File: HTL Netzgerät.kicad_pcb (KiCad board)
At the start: 2 copper layers, 139.7 x 65.7 mm, 62 parts, among them T1 BC547, T2 BC547, T3 BC547, T4 BC547, T5 BC547, T6 BC557, T7 BC557, T8 BC639, X1 AUX1_AC1, X10 C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

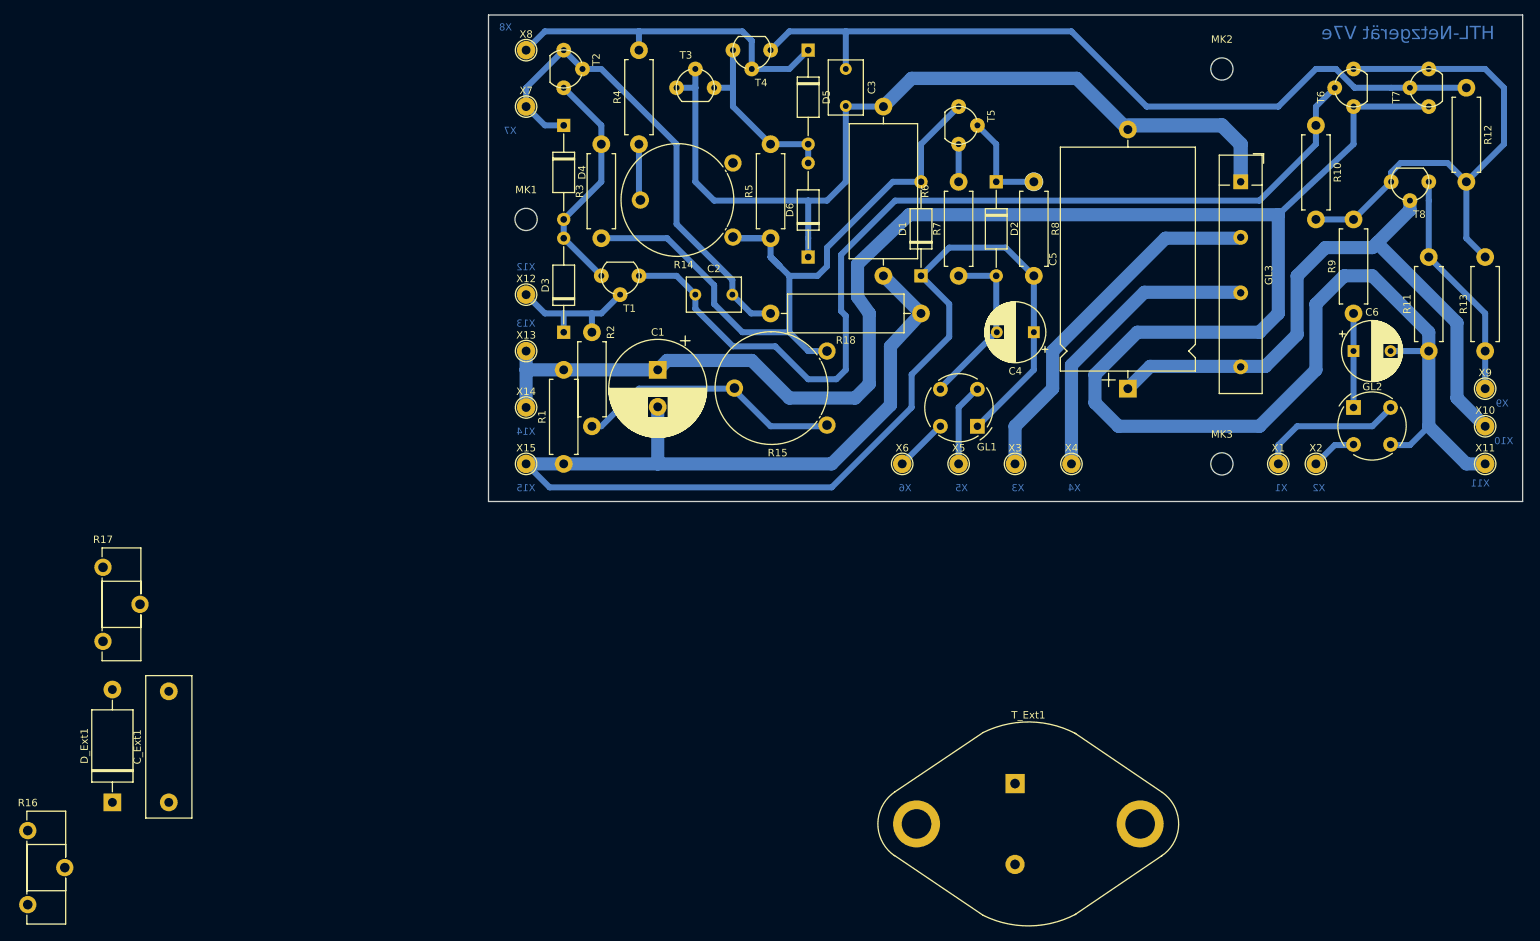
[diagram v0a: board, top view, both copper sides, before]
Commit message: Libs und TODOs aktualisiert
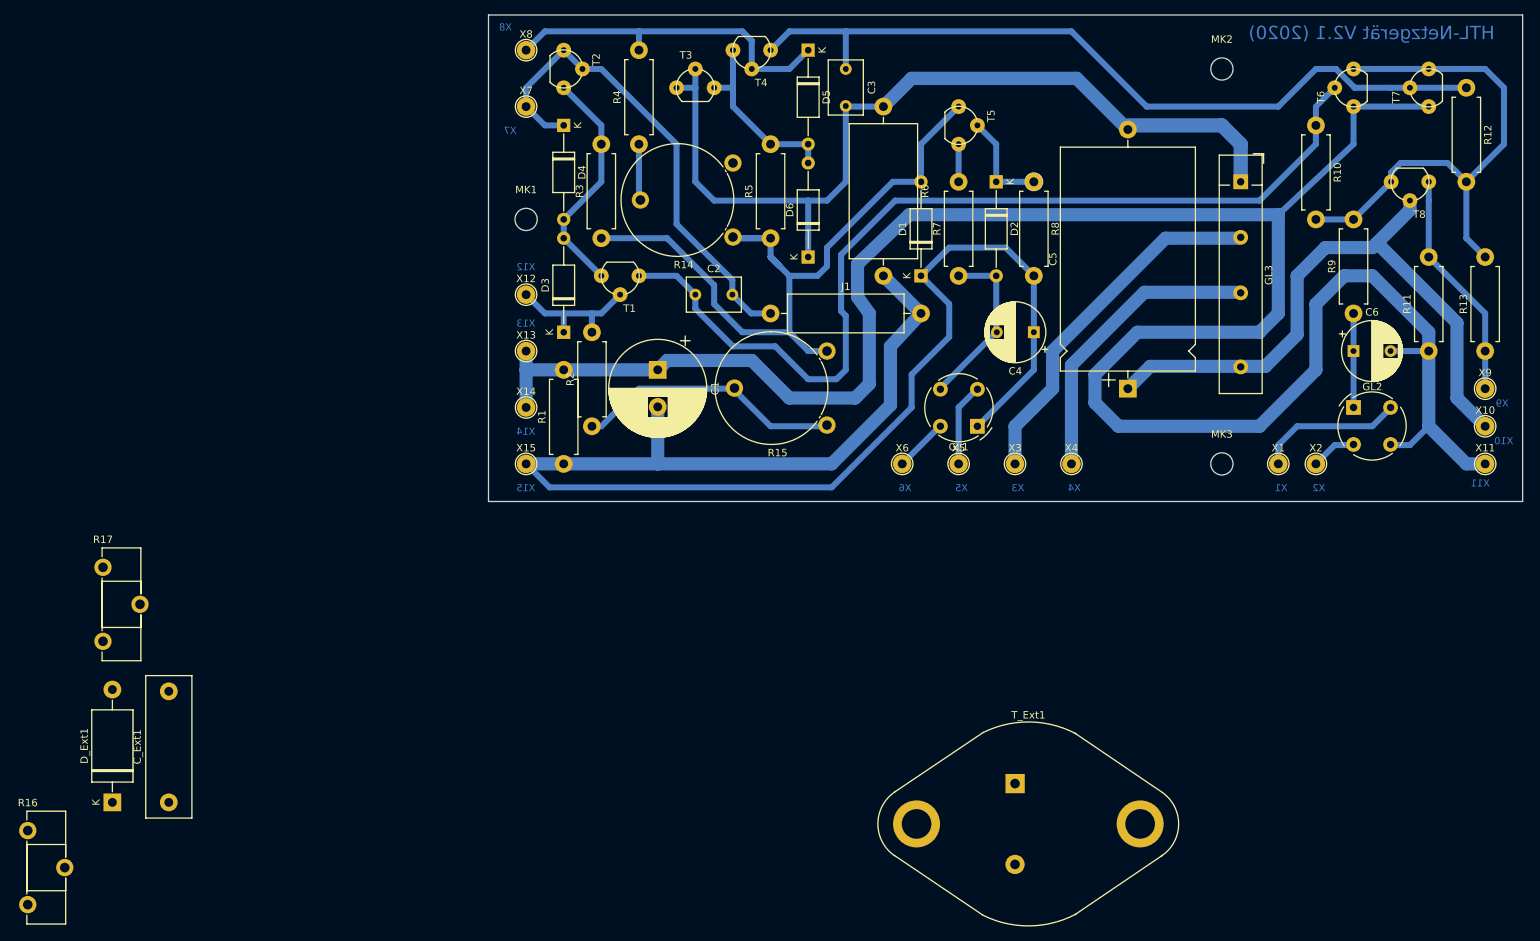
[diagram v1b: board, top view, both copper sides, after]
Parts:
- removed R18: 0R/20.32mm, v5_Resistor_THT:R_Axial_DIN0516_L15.5mm_D5.0mm_P20.32mm_Horizontal
- added J1: 0.7/20.32mm, Resistor_THT:R_Axial_DIN0516_L15.5mm_D5.0mm_P20.32mm_Horizontal, F.Cu at (116.8, 112.5)
- C1: footprint v5_Capacitor_THT:CP_Radial_D13.0mm_P5.00mm -> Capacitor_THT:CP_Radial_D13.0mm_P5.00mm
- C2, C3: footprint v5_Capacitor_THT:C_Rect_L7.2mm_W4.5mm_P5.00mm_FKS2_FKP2_MKS2_MKP2 -> Capacitor_THT:C_Rect_L7.2mm_W4.5mm_P5.00mm_FKS2_FKP2_MKS2_MKP2
- C4, C6: footprint v5_Capacitor_THT:CP_Radial_D8.0mm_P5.00mm -> Capacitor_THT:CP_Radial_D8.0mm_P5.00mm
- C5: footprint v5_Capacitor_THT:CP_Axial_L30.0mm_D18.0mm_P35.00mm_Horizontal -> Capacitor_THT:CP_Axial_L30.0mm_D18.0mm_P35.00mm_Horizontal
- C_Ext1: footprint v5_Capacitor_THT:C_Rect_L19.0mm_W6.0mm_P15.00mm_MKS4 -> Capacitor_THT:C_Rect_L19.0mm_W6.0mm_P15.00mm_MKS4
- D1, D2, D3, D4, D5, D6: footprint v5_Diode_THT:D_A-405_P12.70mm_Horizontal -> Diode_THT:D_A-405_P12.70mm_Horizontal
- D_Ext1: footprint v5_Diode_THT:D_DO-27_P15.24mm_Horizontal -> Diode_THT:D_DO-27_P15.24mm_Horizontal
- GL1, GL2: footprint v5_Diode_THT:Diode_Bridge_Round_D9.0mm -> Diode_THT:Diode_Bridge_Round_D9.0mm
- GL3: footprint v5_Diode_THT:Diode_Bridge_32.0x5.6x17.0mm_P10.0mm_P7.5mm -> Diode_THT:Diode_Bridge_32.0x5.6x17.0mm_P10.0mm_P7.5mm
- MK1, MK2, MK3: footprint v5_MountingHole:MountingHole_3mm -> MountingHole:MountingHole_3mm
- R1, R10, R11, R12, R13, R2, R3, R4, R5, R7, R8, R9: footprint v5_Resistor_THT:R_Axial_DIN0411_L9.9mm_D3.6mm_P12.70mm_Horizontal -> Resistor_THT:R_Axial_DIN0411_L9.9mm_D3.6mm_P12.70mm_Horizontal
- R14, R15: footprint v5_Potentiometer_THT:Potentiometer_Piher_PT-15-V02_Vertical -> Potentiometer_THT:Potentiometer_Piher_PT-15-V02_Vertical
- R16, R17: footprint v5_Potentiometer_THT:Potentiometer_Piher_PT-15-H25_Horizontal -> Potentiometer_THT:Potentiometer_Piher_PT-15-H25_Horizontal
- R6: footprint v5_Resistor_THT:R_Axial_DIN0918_L18.0mm_D9.0mm_P22.86mm_Horizontal -> Resistor_THT:R_Axial_DIN0918_L18.0mm_D9.0mm_P22.86mm_Horizontal
- T_Ext1: footprint v5_Package_TO_SOT_THT:TO-3 -> Package_TO_SOT_THT:TO-3
- X1, X10, X11, X12, X13, X14, X15, X2, X3, X4, X5, X6, X7, X8, X9: footprint v5_TestPoint:TestPoint_THTPad_D2.5mm_Drill1.2mm -> TestPoint:TestPoint_THTPad_D2.5mm_Drill1.2mm
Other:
- board text added: "HTL-Netzgerät V2.1 (2020)"
- board text removed: "HTL-Netzgerät V7e"

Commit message: Einige Korrekturen eingepflegt für Version 2.1
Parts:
- MK1, MK2, MK3: footprint MountingHole:MountingHole_3mm -> MountingHole:MountingHole_3.2mm_M3
- R14, R15: footprint Potentiometer_THT:Potentiometer_Piher_PT-15-V02_Vertical -> HTL_Netzgeraet:Potentiometer_Piher_PT-15-V02_Vertical
- R6: footprint Resistor_THT:R_Axial_DIN0918_L18.0mm_D9.0mm_P22.86mm_Horizontal -> Resistor_THT:R_Axial_DIN0922_L20.0mm_D9.0mm_P30.48mm_Horizontal
- T1, T2, T3, T4, T5, T6, T7, T8: footprint HTL Netzgerät:TO-92 -> HTL_Netzgeraet:TO-92
- X1, X10, X11, X12, X13, X14, X15, X2, X3, X4, X5, X6, X7, X8, X9: footprint TestPoint:TestPoint_THTPad_D2.5mm_Drill1.2mm -> HTL_Netzgeraet:TestPoint_THTPad_D2.5mm_Drill1.25mm
- moved X3 7.62 mm to (157.4, 132.8)
- moved X4 7.62 mm to (149.8, 132.8)
- moved X1 5.08 mm to (190.4, 132.8)
- moved X2 5.08 mm to (185.3, 132.8)
- renumbered R16 to P1, R17 to P2
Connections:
- J1 pad 1: /V_U_Ref -> /0V
- J1 pad 2: /0V -> /V_U_Ref
- X1 pad 1: Net-(GL2-Pad4) -> Net-(GL2-Pad2)
- X2 pad 1: Net-(GL2-Pad2) -> Net-(GL2-Pad4)
- X3 pad 1: Net-(GL3-Pad2) -> Net-(GL3-Pad3)
- X4 pad 1: Net-(GL3-Pad3) -> Net-(GL3-Pad2)
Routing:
- net Net-(R14-Pad2): track 7.62 -> 10.4 mm
- net Net-(R15-Pad2): track 36.0 -> 38.7 mm
- net Net-(GL2-Pad4): track 19.9 -> 18.4 mm

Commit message: Weitere Verbesserungen, Drahtbrücke, Texte, siehe Changelog
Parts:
- GL3: footprint Diode_THT:Diode_Bridge_32.0x5.6x17.0mm_P10.0mm_P7.5mm -> HTL_Netzgeraet:Brueckengleichrichter_p7.4-7.2-9.5mm
- J1: footprint Resistor_THT:R_Axial_DIN0516_L15.5mm_D5.0mm_P20.32mm_Horizontal -> HTL_Netzgeraet:Drahtbruecke_d0.7mm_P20.32mm
- moved C3 20.5 mm to (106.6, 76.9)
- moved J1 20.3 mm to (137.1, 112.5), turned to 180 degrees
- moved GL1 7.18 mm to (139.6, 122.6), turned to 0 degrees
- moved R6 5.68 mm to (129.5, 79.4)
- moved T3 5.08 mm to (104.1, 87.1)
- moved C4 5.08 mm to (147.2, 115.0), turned to 0 degrees
- moved C1 3.59 mm to (99.0, 122.6), turned to 0 degrees
- moved T4 2.54 mm to (114.2, 76.9), turned to 270 degrees
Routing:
- net Net-(GL1-Pad4): track 7.18 -> 16.5 mm
- net /0V: track 202.5 -> 211.4 mm
- net /U_AUX2: track 23.5 -> 30.5 mm
- net /V_I_Ref: track 121.8 -> 115.0 mm
- net Net-(GL1-Pad2): track 11.2 -> 6.21 mm
- net /V_I_FB: track 47.1 -> 42.3 mm
- net Net-(C3-Pad1): track 107.5 -> 112.0 mm
- net /A_-0.6V: track 25.0 -> 21.4 mm
- net Net-(R10-Pad2): track 72.7 -> 69.6 mm
- net /U_OUT: track 310.0 -> 311.1 mm
- net Net-(C2-Pad1): track 130.2 -> 131.2 mm
- net Net-(D2-Pad1): vias 1 -> 0
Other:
- board text removed: "139.5"
- board text removed: "66.0"

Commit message: Fertig zur Produktion, Gerber, Screenshots, Bestückungsdruck, ...
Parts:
- removed C_Ext1: 100n, Capacitor_THT:C_Rect_L19.0mm_W6.0mm_P15.00mm_MKS4
- removed D_Ext1: BY550, Diode_THT:D_DO-27_P15.24mm_Horizontal
- removed P1, P2: POT, Potentiometer_THT:Potentiometer_Piher_PT-15-H25_Horizontal
- removed T_Ext1: 2N3055, Package_TO_SOT_THT:TO-3
- R1, R10, R11, R12, R13, R2, R3, R4, R5, R7, R8, R9: footprint Resistor_THT:R_Axial_DIN0411_L9.9mm_D3.6mm_P12.70mm_Horizontal -> HTL_Netzgeraet:R_Axial_DIN0411_L9.9mm_D3.6mm_P12.70mm_Horizontal
- moved GL1 2.54 mm to (139.6, 120.1)
- moved R9 2.54 mm to (195.5, 109.9)
- moved R14 1.27 mm to (113.0, 92.1)
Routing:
- net Net-(GL1-Pad2): track 6.21 -> 8.75 mm
- net /U_OUT: track 311.1 -> 313.6 mm
- net /U_AUX1: track 12.7 -> 15.2 mm
- net /U_AUX2: track 30.5 -> 28.1 mm
- net Net-(GL1-Pad4): track 16.5 -> 18.7 mm
- net /0V: track 211.4 -> 210.3 mm
- net /U_Main: track 85.1 -> 85.9 mm
- net /V_I_FB: track 42.3 -> 41.8 mm
- net Net-(R14-Pad2): track 10.4 -> 10.9 mm
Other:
- board size 139.7 x 65.7 mm -> 140 x 65 mm
- board text added: "AUX1"
- board text added: "AUX2"
- board text added: "GND"
- board text added: "HTL Steyr"
- board text added: "HTL-Netzgerät Hauptplatine V2.1"
- board text added: "I-POT"
- board text added: "KZ"
- board text added: "MAIN"
- board text added: "OUT"
- board text added: "R5"
- board text added: "Transistor E C B"
- board text added: "U-POT"
